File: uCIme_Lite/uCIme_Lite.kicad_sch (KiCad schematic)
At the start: 4 parts

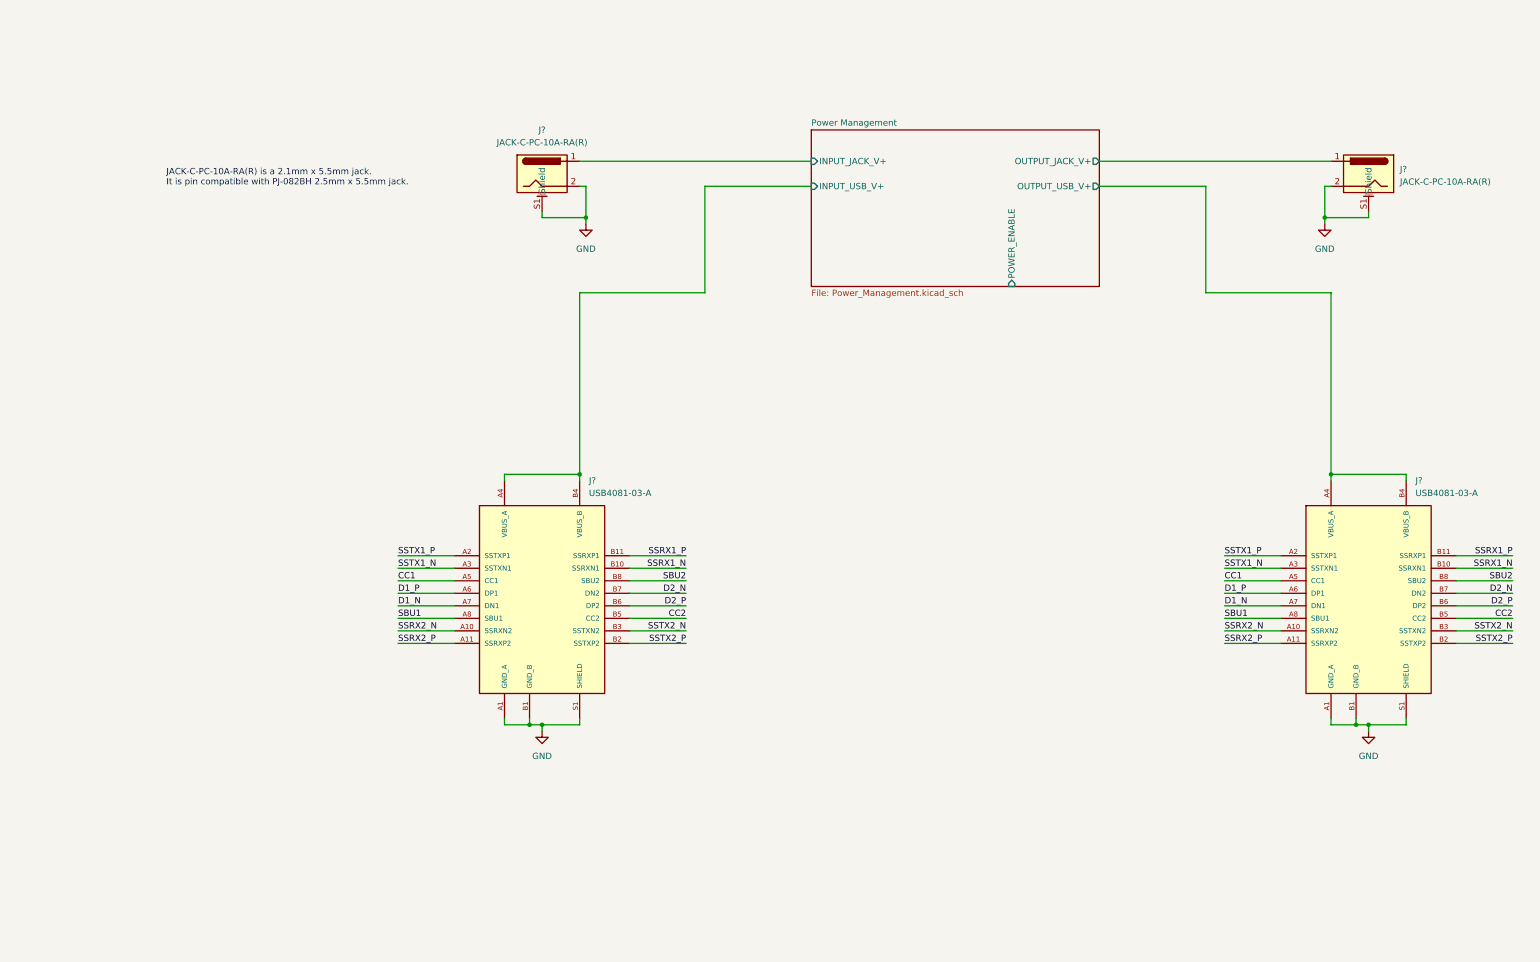
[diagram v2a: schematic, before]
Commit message: lite: Added FTDI USB connector, power supplies and USB differential pair to schematic.
Signed-off-by: Adrien Ricciardi <aricciardi@baylibre.com>
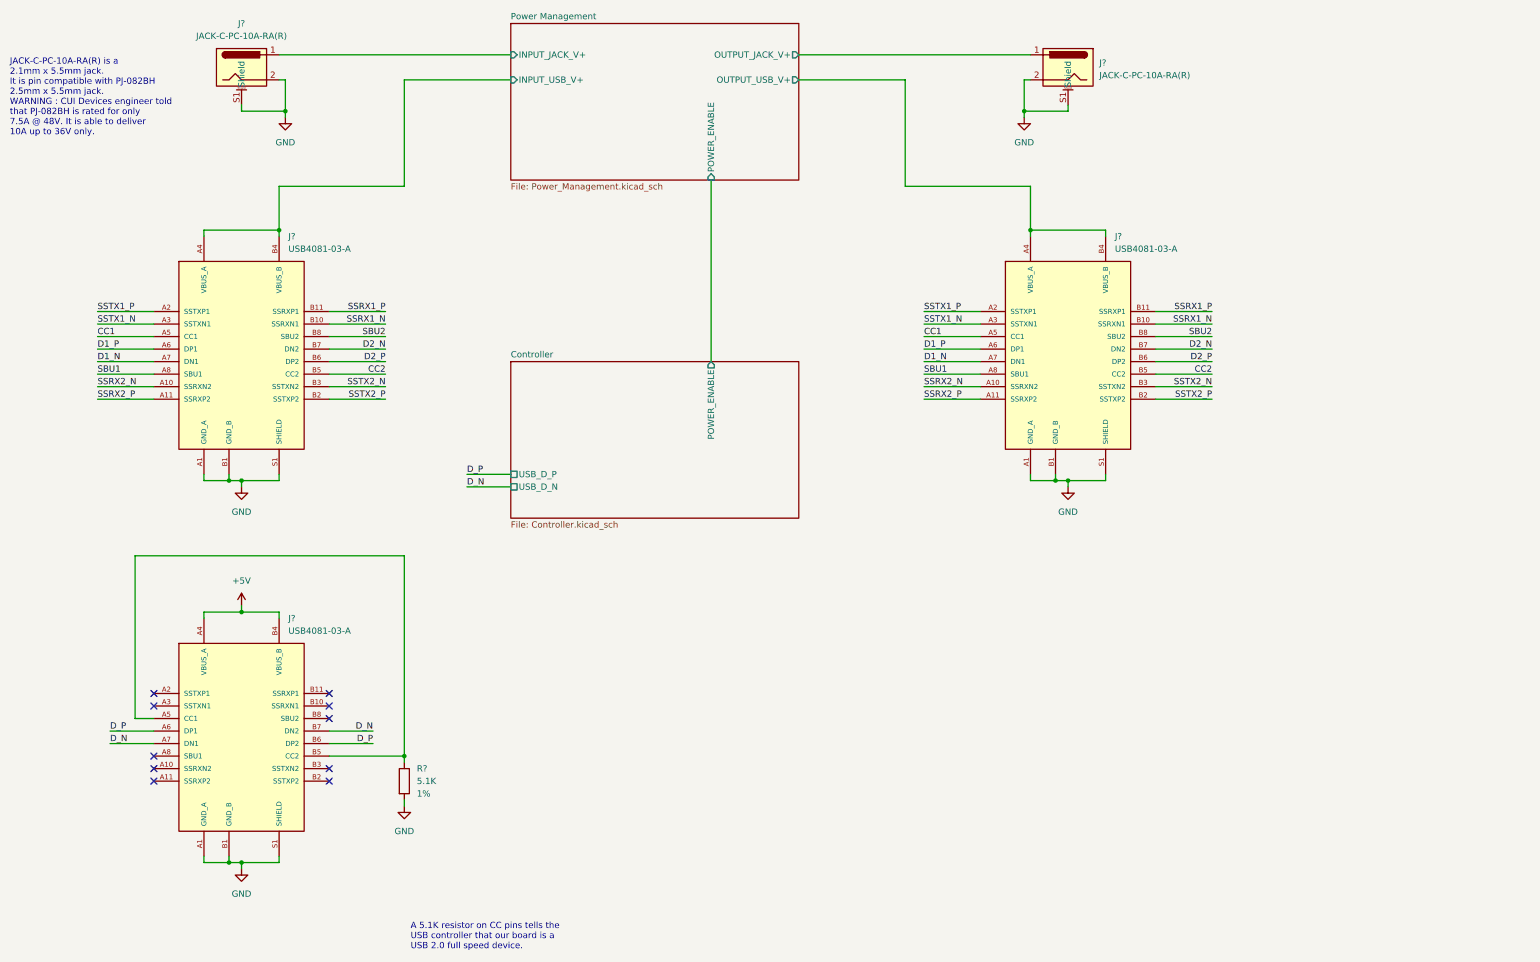
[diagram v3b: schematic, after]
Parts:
- added J?: USB4081-03-A, USB4081:USB4081-03-A, symbol USB4081:USB4081-03-A
- added R?: 5.1K, Resistor_SMD:R_0603_1608Metric, symbol Device:R
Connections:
- net GND: now also J?.A1 (GND_A), J?.A12 (GND_A), J?.B1 (GND_B), J?.B12 (GND_B), J?.S1 (SHIELD), J?.S2 (SHIELD), J?.S3 (SHIELD), J?.S4 (SHIELD), J?.S5 (SHIELD), J?.S6 (SHIELD), R?.2
- net VBUS_A renamed +5V
- net +5V: now also J?.A4 (VBUS_A), J?.A9 (VBUS_A), J?.B4 (VBUS_B), J?.B9 (VBUS_B)
- new net: J?.A5 (CC1), J?.B5 (CC2), R?.1
- new net D_N: J?.A7 (DN1), J?.B7 (DN2)
- new net D_P: J?.A6 (DP1), J?.B6 (DP2)
- no-connect marks 0 -> 10
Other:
- added sheet Controller (Controller.kicad_sch)
- note added: "A 5.1K resistor on CC pins tells the USB controller that our board is a USB 2.0 full speed device."
- note added: "JACK-C-PC-10A-RA(R) is a 2.1mm x 5.5mm jack. It is pin compatible with PJ-082BH 2.5mm x 5.5mm jack. WARNING : CUI Devices engineer told that PJ-082BH is rated for only 7.5A @ 48V. It is able to deliver 10A up to 36V only."
- note removed: "JACK-C-PC-10A-RA(R) is a 2.1mm x 5.5mm jack. It is pin compatible with PJ-082BH 2.5mm x 5.5mm jack."
- moved on the sheet: J?

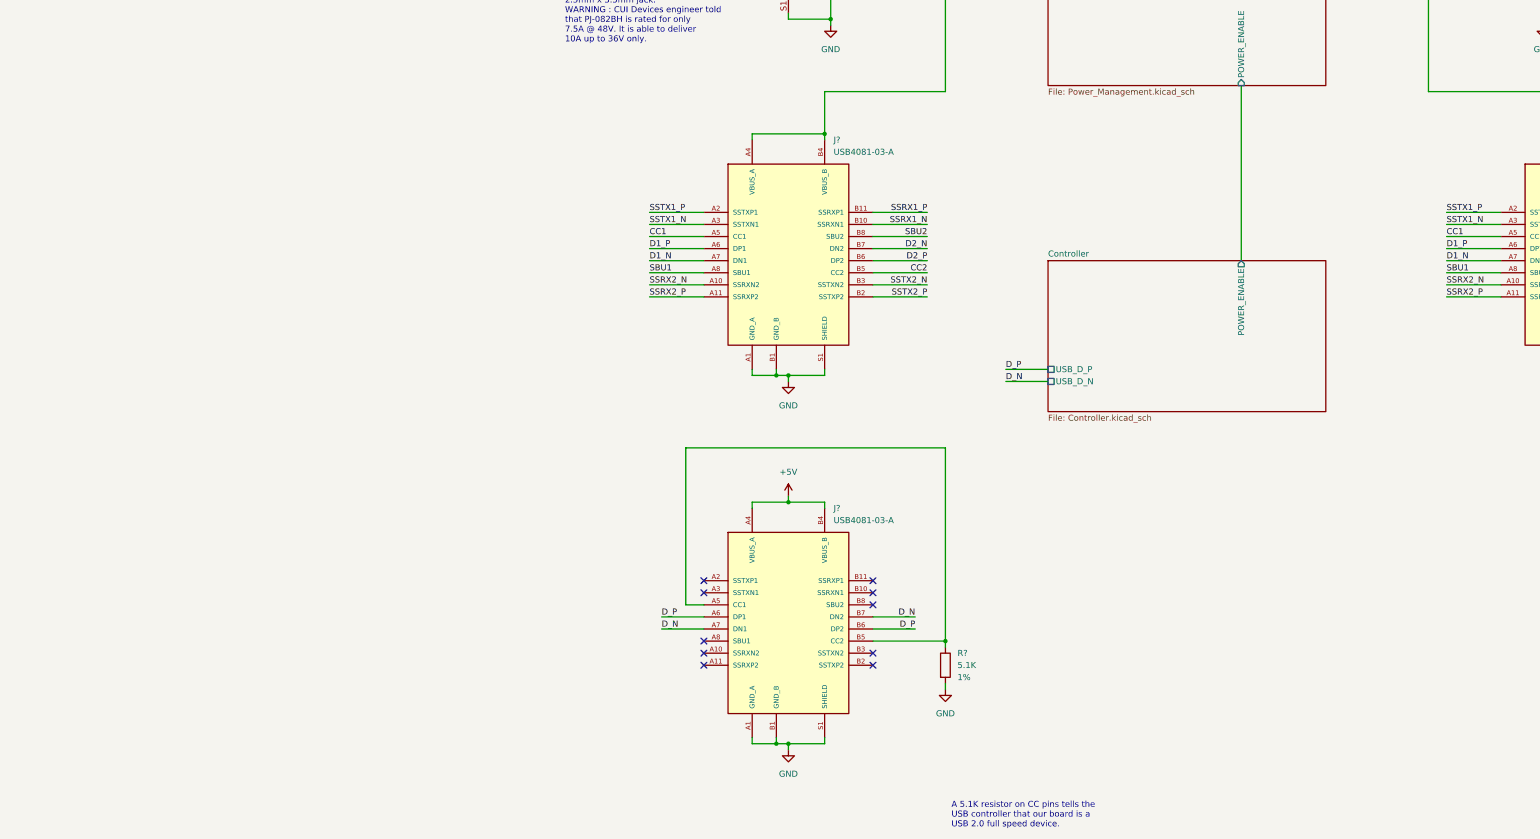
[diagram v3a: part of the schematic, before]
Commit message: lite: Added serial and USB connectors. A voltage translator is provided on the serial ports for the user to select the appropriate board voltage. No voltage translator is provided on the FTDI GPIO pins because they are meant to be used with custom extension boards.
Signed-off-by: Adrien Ricciardi <aricciardi@baylibre.com>
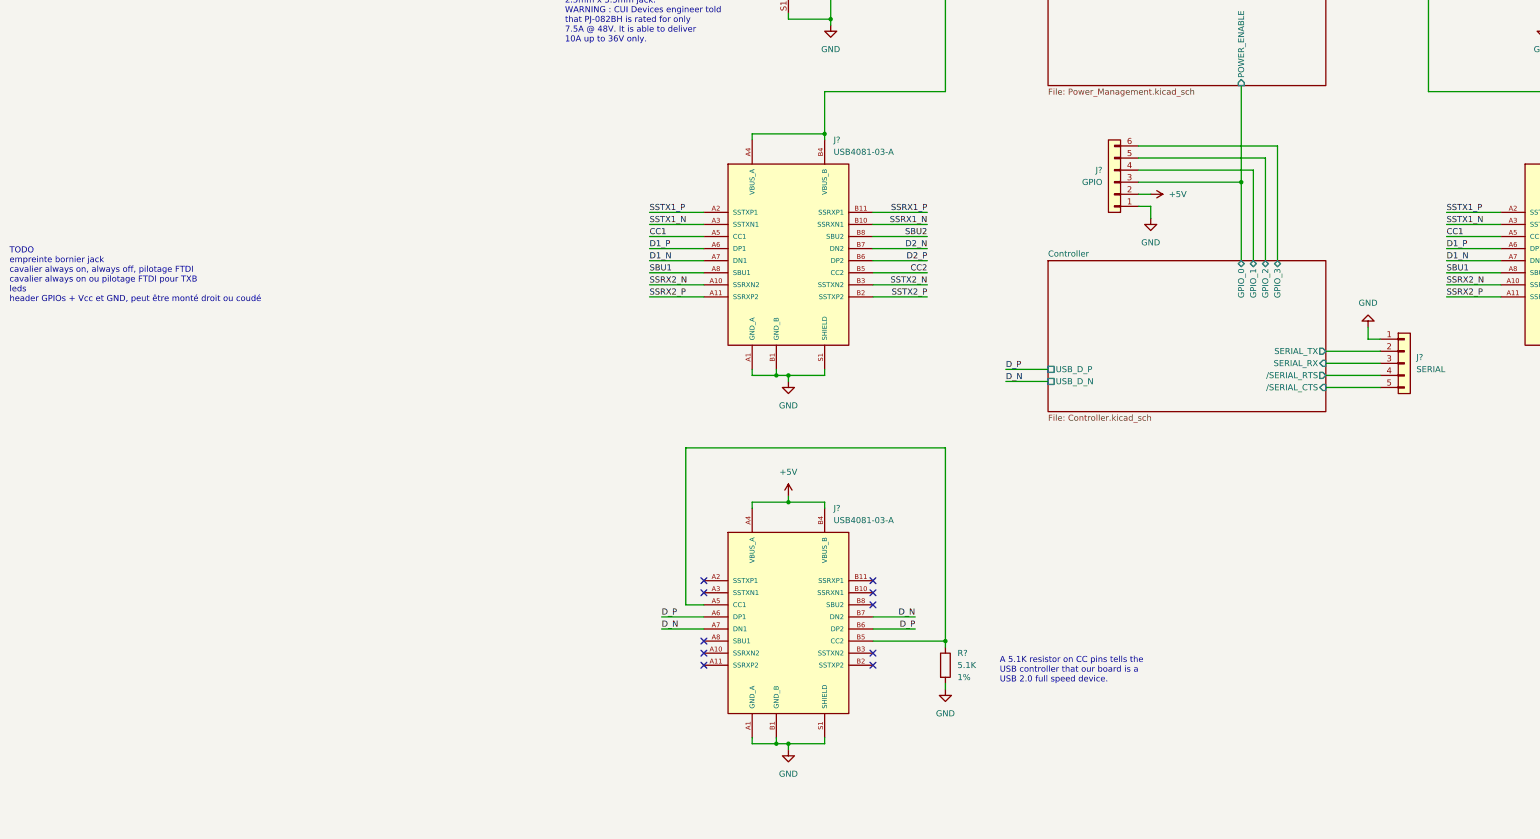
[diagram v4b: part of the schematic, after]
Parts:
- added J?: GPIO, symbol Connector_Generic:Conn_01x06
- added J?: SERIAL, symbol Connector_Generic:Conn_01x05
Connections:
- net +5V: now also J?.2 (Pin_2)
- net GND: now also J?.1 (Pin_1), J?.1 (Pin_1)
- new net Controller/GPIO_0: J?.3 (Pin_3)
- new net Controller/GPIO_1: J?.4 (Pin_4)
- new net Controller/GPIO_2: J?.5 (Pin_5)
- new net Controller/GPIO_3: J?.6 (Pin_6)
- new net Controller/SERIAL_RX: J?.3 (Pin_3)
- new net Controller/SERIAL_TX: J?.2 (Pin_2)
- new net Controller//SERIAL_CTS: J?.5 (Pin_5)
- new net Controller//SERIAL_RTS: J?.4 (Pin_4)
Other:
- sheet Controller ports: added GPIO_0, GPIO_1, GPIO_2, GPIO_3, SERIAL_RX, SERIAL_TX, /SERIAL_CTS, /SERIAL_RTS; removed POWER_ENABLE
- note added: "TODO empreinte bornier jack cavalier always on, always off, pilotage FTDI cavalier always on ou pilotage FTDI pour TXB leds header GPIOs + Vcc et GND, peut être monté droit ou coudé"

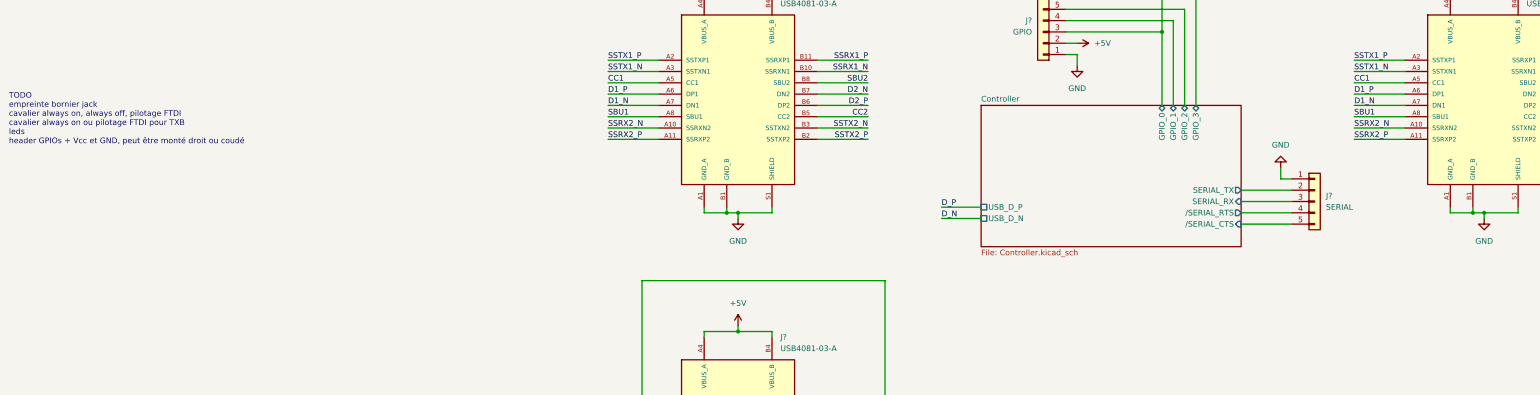
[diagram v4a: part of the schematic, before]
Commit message: lite: Added the LDOs for the serial port voltage translator.
Signed-off-by: Adrien Ricciardi <aricciardi@baylibre.com>
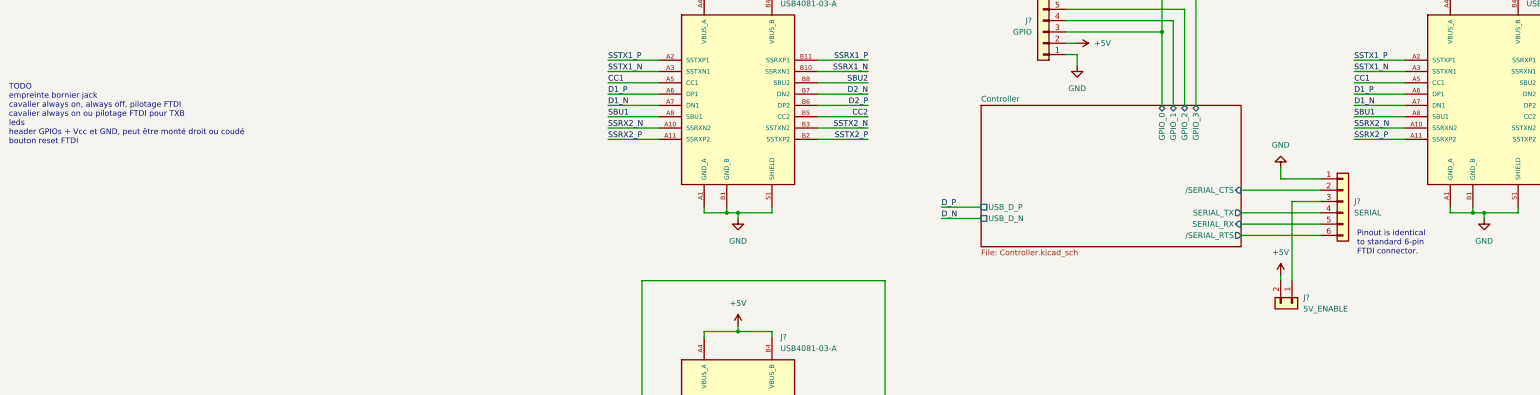
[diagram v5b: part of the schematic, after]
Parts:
- removed J?: SERIAL, symbol Connector_Generic:Conn_01x05
- added J?: 5V_ENABLE, Connector_PinHeader_2.54mm:PinHeader_1x02_P2.54mm_Horizontal, symbol Connector_Generic:Conn_01x02
- added J?: SERIAL, Connector_PinHeader_2.54mm:PinHeader_1x06_P2.54mm_Horizontal, symbol Connector_Generic:Conn_01x06
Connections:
- net +5V: now also J?.2 (Pin_2)
- net Controller/SERIAL_RX: now also J?.5 (Pin_5)
- net Controller/SERIAL_TX: now also J?.4 (Pin_4)
- net Controller//SERIAL_CTS: now also J?.2 (Pin_2)
- net Controller//SERIAL_RTS: now also J?.6 (Pin_6)
- net GND: now also J?.1 (Pin_1)
- new net: J?.1 (Pin_1), J?.3 (Pin_3)
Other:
- note added: "Pinout is identical to standard 6-pin FTDI connector."
- note added: "TODO empreinte bornier jack cavalier always on, always off, pilotage FTDI cavalier always on ou pilotage FTDI pour TXB leds header GPIOs + Vcc et GND, peut être monté droit ou coudé bouton reset FTDI"
- note removed: "TODO empreinte bornier jack cavalier always on, always off, pilotage FTDI cavalier always on ou pilotage FTDI pour TXB leds header GPIOs + Vcc et GND, peut être monté droit ou coudé"

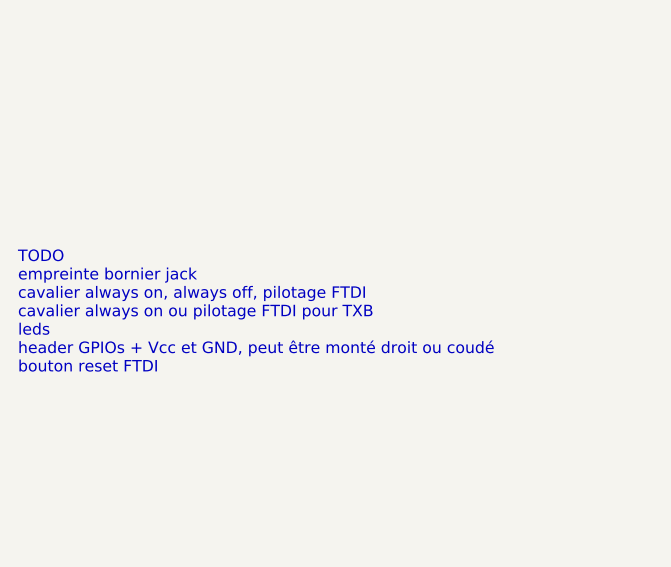
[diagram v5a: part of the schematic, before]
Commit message: lite: Added jumpers to control the power channel mode (always enabled, always disabled or controlled by a FTDI GPIO).
Signed-off-by: Adrien Ricciardi <aricciardi@baylibre.com>
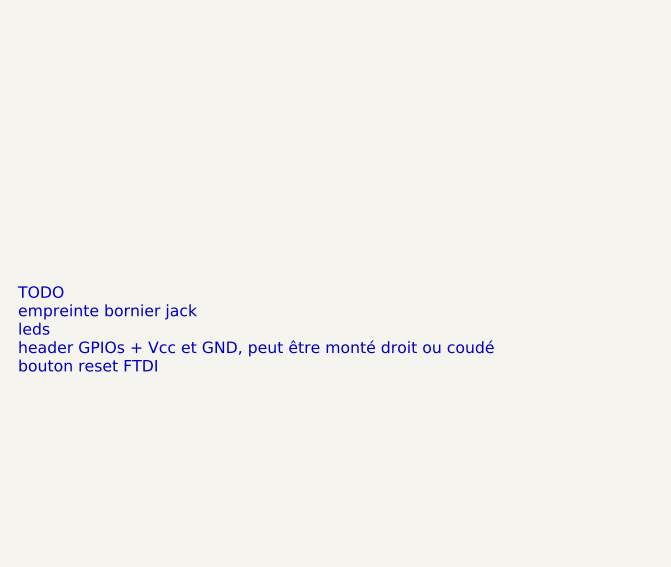
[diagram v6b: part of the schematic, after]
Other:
- note added: "TODO empreinte bornier jack leds header GPIOs + Vcc et GND, peut être monté droit ou coudé bouton reset FTDI"
- note removed: "TODO empreinte bornier jack cavalier always on, always off, pilotage FTDI cavalier always on ou pilotage FTDI pour TXB leds header GPIOs + Vcc et GND, peut être monté droit ou coudé bouton reset FTDI"
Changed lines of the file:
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@@
     (stroke (width 0) (type default) (color 0 0 0 0))
   )
-  (text "TODO\nempreinte bornier jack\ncavalier always on, always off, pilotage FTDI\ncavalier always on ou pilotage FTDI pour TXB\nleds\nheader GPIOs + Vcc et GND, peut être monté droit ou coudé\nbouton reset FTDI"
+  (text "TODO\nempreinte bornier jack\nleds\nheader GPIOs + Vcc et GND, peut être monté droit ou coudé\nbouton reset FTDI"
     (at -101.6 95.25 0)
     (effects (font (size 1.27 1.27)) (justify left bottom))
@@
       (reference "#PWR?") (unit 1) (value "+5V") (footprint "")
     )
+    (path "/b72074d7-db6e-4ce2-896d-216adccf1d19/1551daf5-2b8f-41bd-a447-3909d1cc7472"
+      (reference "#PWR?") (unit 1) (value "GND") (footprint "")
+    )
     (path "/1565d401-3cd3-41df-a409-a6814a312f92"
       (reference "#PWR?") (unit 1) (value "GND") (footprint "")
@@
       (reference "#PWR?") (unit 1) (value "GND") (footprint "")
     )
+    (path "/b72074d7-db6e-4ce2-896d-216adccf1d19/1f12c4d3-7a52-4ecf-824b-1dc287eac224"
+      (reference "#PWR?") (unit 1) (value "+3.3V") (footprint "")
+    )
     (path "/29b4325a-46c6-4d8a-95bf-1c9b8d71c824"
       (reference "#PWR?") (unit 1) (value "GND") (footprint "")
@@
       (reference "#PWR?") (unit 1) (value "GND") (footprint "")
     )
-    (path "/85cb8885-4077-4bc3-b1fe-5b247ce2fc7e/e001be2f-98a4-4c84-be96-1748147eebb9"
-      (reference "#PWR?") (unit 1) (value "GND") (footprint "")
-    )
     (path "/85cb8885-4077-4bc3-b1fe-5b247ce2fc7e/eaa1a394-bd54-4355-a602-c6e32f8520e7"
       (reference "#PWR?") (unit 1) (value "GND") (footprint "")
@@
       (reference "J?") (unit 1) (value "USB4081-03-A") (footprint "USB4081:USB4081-03-A")
     )
+    (path "/b72074d7-db6e-4ce2-896d-216adccf1d19/e745c796-8049-4c27-917b-32ab16991e40"
+      (reference "J?") (unit 1) (value "SERIAL_MODE") (footprint "")
+    )
     (path "/b72074d7-db6e-4ce2-896d-216adccf1d19/24df8571-9618-4f38-9191-19c2d92e80ea"
       (reference "Q?") (unit 1) (value "BUK7M27-80EX") (footprint "Package_TO_SOT_SMD:LFPAK33")
@@
       (reference "R?") (unit 1) (value "10K") (footprint "Resistor_SMD:R_0603_1608Metric")
     )
-    (path "/85cb8885-4077-4bc3-b1fe-5b247ce2fc7e/52f489fc-ba0c-4b82-b082-bf914ccaa024"
-      (reference "R?") (unit 1) (value "10K") (footprint "Resistor_SMD:R_0603_1608Metric")
-    )
     (path "/85cb8885-4077-4bc3-b1fe-5b247ce2fc7e/612384df-c24f-4193-b683-98780337f737"
       (reference "R?") (unit 1) (value "6K") (footprint "Resistor_SMD:R_0603_1608Metric")
@@
       (reference "R?") (unit 1) (value "27") (footprint "Resistor_SMD:R_0603_1608Metric")
     )
+    (path "/b72074d7-db6e-4ce2-896d-216adccf1d19/eea35a60-b973-44cd-972b-f007e7d59fef"
+      (reference "R?") (unit 1) (value "10K") (footprint "Resistor_SMD:R_0603_1608Metric")
+    )
     (path "/85cb8885-4077-4bc3-b1fe-5b247ce2fc7e/fb48803c-800b-475d-b7e9-d3a267fee279"
